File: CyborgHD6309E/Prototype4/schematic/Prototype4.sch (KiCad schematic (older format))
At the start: 20 parts, among them J1 Conn_AVR_UPDI, SW1 TSD1265, U1 ATmega4809-P, U2 HM628128DLP-5, U3 HD63C09E, U4 ATtiny412-SS, U5 CD74HCT30, U6 CD74HCT688

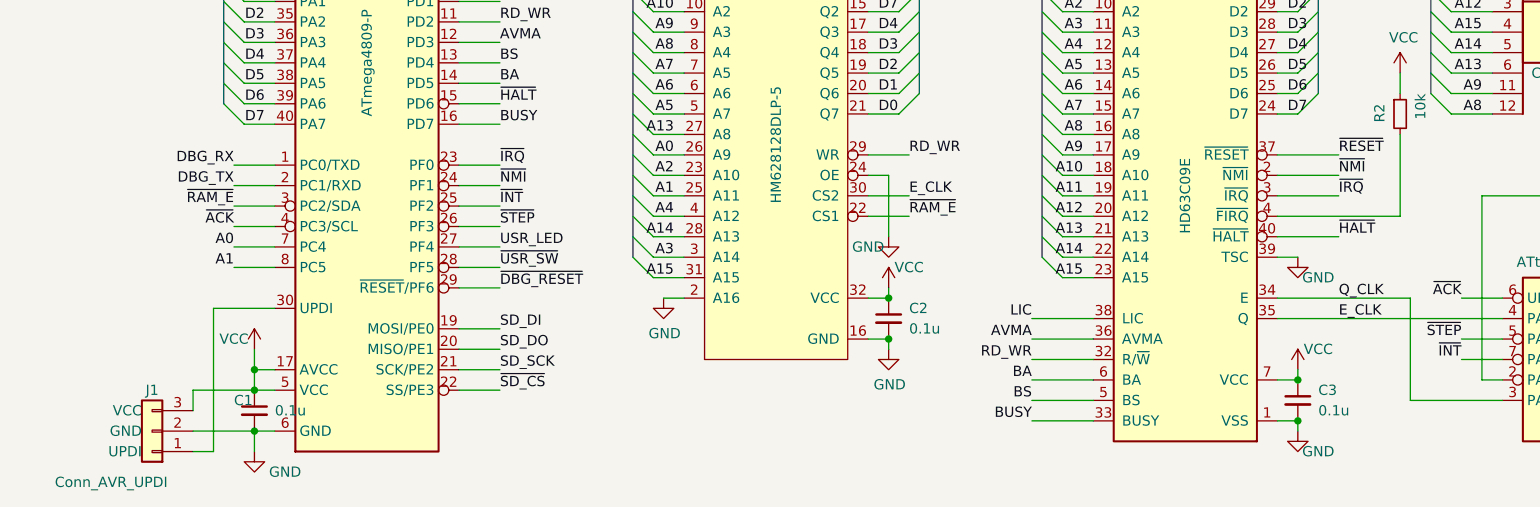
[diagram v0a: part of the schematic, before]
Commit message: [CyborgHD6309E] Modify Prototype4 pin maps to upcomming Prototype5
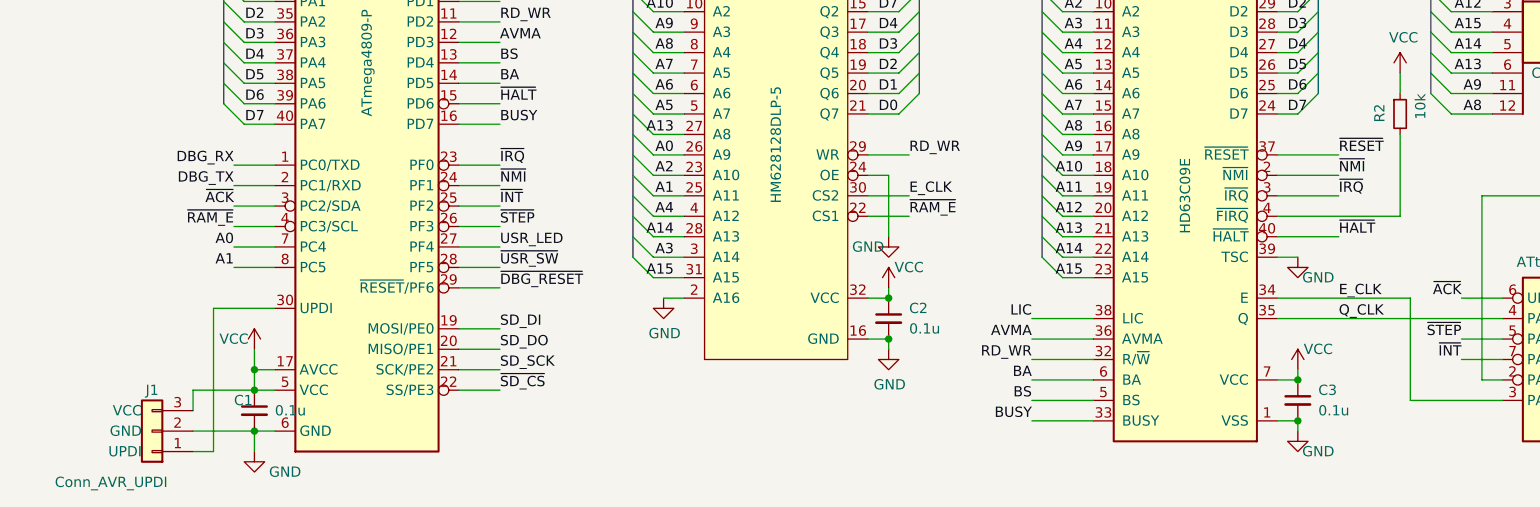
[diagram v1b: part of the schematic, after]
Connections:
- net E_CLK: now also U3.34 (E), U4.3 (PA7); no longer U3.35 (Q), U4.4 (PA1)
- net Q_CLK: now also U3.35 (Q), U4.4 (PA1); no longer U3.34 (E), U4.3 (PA7)
- net ~ACK~: now also U1.3 (PC2/SDA); no longer U1.4 (PC3/SCL)
- net ~RAM_E~: now also U1.4 (PC3/SCL); no longer U1.3 (PC2/SDA)
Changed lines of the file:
@@
 Sheet 1 1
 Title "CyborgHD6309E Prototype4"
-Date "2021-01-29"
-Rev "4"
+Date "2021-02-05"
+Rev "5"
 Comp "Tadashi G. Takaoka"
 Comment1 ""
@@
 Text Label 5150 2950 0    50   ~ 0
 RD_WR
+Text Label 7250 3650 0    50   ~ 0
+E_CLK
 Text Label 7250 3750 0    50   ~ 0
-E_CLK
-Text Label 7250 3650 0    50   ~ 0
 Q_CLK
 Text Label 5750 3750 2    50   ~ 0
@@
 Wire Wire Line
 	2950 2100 3150 2100
+Text Label 1850 3200 2    50   ~ 0
+~ACK~
+Wire Wire Line
+	2950 2200 3150 2200
+Wire Wire Line
+	2950 2800 3150 2800
 Text Label 1850 3300 2    50   ~ 0
-~ACK~
-Wire Wire Line
-	2950 2200 3150 2200
-Wire Wire Line
-	2950 2800 3150 2800
-Text Label 1850 3200 2    50   ~ 0
 ~RAM_E~
 Wire Wire Line
